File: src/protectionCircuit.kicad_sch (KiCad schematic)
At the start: 21 parts, among them M1 CSD19534Q5A, M2 CSD19534Q5A, M3 CSD19534Q5A, U1 LM74910QRGERQ1

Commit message: Restored powerDistribution PCB files to commit 2fb1c3a
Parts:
- removed M3: CSD19534Q5A, powerDristributionBoard-import-fps:DQJ8, symbol Schlib1:CSD19534Q5A
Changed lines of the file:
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@@
-	)
-	(symbol
-		(lib_id "Schlib1:CSD19534Q5A")
-		(at 233.68 20.32 0)
-		(unit 1)
-		(body_style 1)
-		(exclude_from_sim no)
-		(in_bom yes)
-		(on_board yes)
-		(in_pos_files yes)
-		(dnp no)
-		(property "Reference" "M3"
-			(at 241.3 20.32 0)
-			(show_name no)
-			(do_not_autoplace no)
-			(effects
-				(font
-					(size 1.27 1.27)
-				)
-				(justify left bottom)
-			)
-		)
-		(property "Value" "CSD19534Q5A"
-			(at 241.3 35.56 0)
-			(show_name no)
-			(do_not_autoplace no)
-			(effects
-				(font
-					(size 1.27 1.27)
-				)
-				(justify left bottom)
-			)
-		)
-		(property "Footprint" "powerDristributionBoard-import-fps:DQJ8"
-			(at 233.68 20.32 0)
-			(hide yes)
-			(show_name no)
-			(do_not_autoplace no)
-			(effects
-				(font
-					(size 1.27 1.27)
-				)
-			)
-		)
-		(property "Datasheet" ""
-			(at 233.68 20.32 0)
-			(hide yes)
-			(show_name no)
-			(do_not_autoplace no)
-			(effects
-				(font
-					(size 1.27 1.27)
-				)
-			)
-		)
-		(property "Description" "100-V, N channel NexFETâ„¢ power MOSFET, single SON 5 mm x 6 mm, 15.1 mOhm 8-VSONP -55 to 150"
-			(at 233.68 20.32 0)
-			(hide yes)
-			(show_name no)
-			(do_not_autoplace no)
-			(effects
-				(font
-					(size 1.27 1.27)
-				)
-			)
-		)
-		(property "COPYRIGHT" "Copyright (C) 2026 Ultra Librarian. All rights reserved."
-			(at 233.68 20.32 0)
-			(hide yes)
-			(show_name no)
-			(do_not_autoplace no)
-			(effects
-				(font
-					(size 1.27 1.27)
-				)
-				(justify left bottom)
-			)
-		)
-		(property "MANUFACTURER_NAME" "Texas Instruments"
-			(at 233.68 20.32 0)
-			(hide yes)
-			(show_name no)
-			(do_not_autoplace no)
-			(effects
-				(font
-					(size 1.27 1.27)
-				)
-				(justify left bottom)
-			)
-		)
-		(property "MANUFACTURER_PART_NUMBER" "CSD19534Q5A"
-			(at 233.68 20.32 0)
-			(hide yes)
-			(show_name no)
-			(do_not_autoplace no)
-			(effects
-				(font
-					(size 1.27 1.27)
-				)
-				(justify left bottom)
-			)
-		)
-		(property "REFDES" "RefDes"
-			(at 254 7.62 0)
-			(hide yes)
-			(show_name no)
-			(do_not_autoplace no)
-			(effects
-				(font
-					(size 1.27 1.27)
-				)
-				(justify left bottom)
-			)
-		)
-		(property "TYPE" "Type"
-			(at 254 10.16 0)
-			(hide yes)
-			(show_name no)
-			(do_not_autoplace no)
-			(effects
-				(font
-					(size 1.27 1.27)
-				)
-				(justify left bottom)
-			)
-		)
-		(pin "4"
-		)
-		(pin "1"
-		)
-		(pin "2"
-		)
-		(pin "3"
-		)
-		(pin "5"
-		)
-		(pin "6"
-		)
-		(pin "7"
-		)
-		(pin "8"
-		)
-		(instances
-			(project "powerDristributionBoard"
-				(path "/501e9f3f-9bfa-47dd-b56d-5fd6974f0d03/decf1042-8545-4374-a825-63213b68d513"
-					(reference "M3")
-					(unit 1)
-				)
-			)
-		)
 	)
 	(symbol

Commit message: Edited the protection circuit
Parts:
- added D1: TVS, symbol Diode:SMAJ6.5CA
- added R_IMON: 6.04k 1%, Resistor_SMD:R_0603_1608Metric, symbol Device:R_Small_US
- renumbered Ccs+1 to Ccs+, Cscp1 to Ciscp
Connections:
- net GND: now also D1.1 (A1), R_IMON.2
- net Vin: now also D1.2 (A2)
- net ENABLE: now reaches Ccap1.2, Cvs1.1, M1.5 (D), M1.6 (D), M1.7 (D), M1.8 (D), R18.1, R_ISCP1.1, Rset1.1, U1.22 (VS), U1.24 (C)
- net ENABLE: now also U1.6 (EN), U1.7 (*SLEEP)
- net Breakout Pin (For MCU): now reaches U1.10 (IMON)
- net Breakout Pin (For MCU): now also R_IMON.1
- no-connect marks 3 -> 5
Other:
- moved on the sheet: C_dvdt1, Ccap1, Ccs+, Ciscp, Cout1, Ctmr1, Cuv1, Cvin1, Cvs1, M1, M2, R18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

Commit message: Added many footprints
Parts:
- removed R18: 5mOhm, powerDristributionBoard-import-fps:CSNL2010, symbol Schlib1:CSNL2010
- added R18: 5mOhms, PowerPCB_Footprints:CSNL2010, symbol Device:R_Trim
- M1, M2: footprint powerDristributionBoard-import-fps:DQJ8 -> PowerPCB_Footprints:CSD19534Q5A
- U1: footprint powerDristributionBoard-import-fps:VQFN24_RGE-T_TEX-L -> PowerPCB_Footprints:LM74910QRGERQ1
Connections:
- net ENABLE: now also R18.1
- net at Ccs+.2, Ciscp.2, M2.1 (S)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: now also R18.2
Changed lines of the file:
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@@
 	(generator_version "10.0")
 	(paper "A")
+	(rectangle
+		(start 33.02 54.61)
+		(end 48.26 66.04)
+		(stroke
+			(width 0)
+			(type solid)
+			(color 255 8 21 1)
+		)
+		(fill
+			(type none)
+		)
+	)
+	(rectangle
+		(start 232.41 53.34)
+		(end 247.65 64.77)
+		(stroke
+			(width 0)
+			(type solid)
+			(color 255 8 21 1)
+		)
+		(fill
+			(type none)
+		)
+	)
 	(junction
 		(at 224.79 53.34)
@@
 	)
 	(junction
-		(at 194.31 50.8)
-		(diameter 0)
-		(color 0 0 0 0)
-	)
-	(junction
 		(at 165.1 91.44)
 		(diameter 0)
@@
 	)
 	(junction
-		(at 176.53 50.8)
-		(diameter 0)
-		(color 0 0 0 0)
-	)
-	(junction
 		(at 165.1 50.8)
 		(diameter 0)
@@
 	)
 	(junction
+		(at 176.53 50.8)
+		(diameter 0)
+		(color 0 0 0 0)
+	)
+	(junction
 		(at 49.53 106.68)
 		(diameter 0)
@@
 	)
 	(junction
+		(at 194.31 50.8)
+		(diameter 0)
+		(color 0 0 0 0)
+	)
+	(junction
 		(at 107.95 53.34)
 		(diameter 0)
@@
 	(wire
 		(pts
-			(xy 176.53 50.8) (xy 179.07 50.8)
+			(xy 176.53 50.8) (xy 181.61 50.8)
 		)
 		(stroke
@@
 	(wire
 		(pts
-			(xy 194.31 50.8) (xy 191.77 50.8)
+			(xy 194.31 50.8) (xy 189.23 50.8)
 		)
 		(stroke
@@
 			)
 		)
-		(property "Footprint" "powerDristributionBoard-import-fps:DQJ8"
+		(property "Footprint" "PowerPCB_Footprints:CSD19534Q5A"
 			(at 82.55 48.26 0)
 			(hide yes)
@@
 			)
 		)
-		(property "Footprint" "powerDristributionBoard-import-fps:DQJ8"
+		(property "Footprint" "PowerPCB_Footprints:CSD19534Q5A"
 			(at 199.39 48.26 0)
 			(hide yes)
@@
 	)
 	(symbol
-		(lib_id "Schlib1:CSNL2010")
-		(at 179.07 50.8 0)
+		(lib_id "Device:R_Small_US")
+		(at 165.1 72.39 0)
 		(unit 1)
 		(body_style 1)
@@
 		(in_pos_files yes)
 		(dnp no)
-		(property "Reference" "R18"
-			(at 181.356 49.276 0)
+		(fields_autoplaced yes)
+		(property "Reference" "R_ISCP1"
+			(at 167.64 71.1199 0)
 			(show_name no)
 			(do_not_autoplace no)
@@
 					(size 1.27 1.27)
 				)
-				(justify left bottom)
+				(justify left)
 			)
 		)
-		(property "Value" "5mOhm"
-			(at 181.61 55.88 0)
+		(property "Value" "952 1%"
+			(at 167.64 73.6599 0)
 			(show_name no)
 			(do_not_autoplace no)
@@
 					(size 1.27 1.27)
 				)
-				(justify left bottom)
+				(justify left)
 			)
 		)
-		(property "Footprint" "powerDristributionBoard-import-fps:CSNL2010"
-			(at 179.07 50.8 0)
+		(property "Footprint" "Resistor_SMD:R_0603_1608Metric"
+			(at 165.1 72.39 0)
 			(hide yes)
 			(show_name no)
@@
 		)
 		(property "Datasheet" ""
-			(at 179.07 50.8 0)
-			(hide yes)
-			(show_name no)
-			(do_not_autoplace no)
-			(effects
-				(font
-					(size 1.27 1.27)
-				)
-			)
-		)
-		(property "Description" ""
-			(at 179.07 50.8 0)
-			(hide yes)
-			(show_name no)
-			(do_not_autoplace no)
-			(effects
-				(font
-					(size 1.27 1.27)
-				)
-			)
-		)
-		(property "COPYRIGHT" "Copyright (C) 2025 Ultra Librarian. All rights reserved."
-			(at 179.07 50.8 0)
-			(hide yes)
-			(show_name no)
-			(do_not_autoplace no)
-			(effects
-				(font
-					(size 1.27 1.27)
-				)
-				(justify left bottom)
-			)
-		)
-		(property "MANUFACTURER_NAME" "Susumu"
-			(at 179.07 50.8 0)
-			(hide yes)
-			(show_name no)
-			(do_not_autoplace no)
-			(effects
-				(font
-					(size 1.27 1.27)
-				)
-				(justify left bottom)
-			)
-		)
-		(property "MANUFACTURER_PART_NUMBER" "PRL1632-R005-F-T1"
-			(at 179.07 50.8 0)
-			(hide yes)
-			(show_name no)
-			(do_not_autoplace no)
-			(effects
-				(font
-					(size 1.27 1.27)
-				)
-				(justify left bottom)
-			)
-		)
-		(property "TYPE" ""
-			(at 185.42 57.785 0)
+			(at 165.1 72.39 0)
 			(hide yes)
 			(show_name no)
@@
 					(size 1.27 1.27)
 				)
-				(justify left bottom)
 			)
 		)
-		(property "REFDES" ""
-			(at 184.785 46.99 0)
+		(property "Description" "Resistor, small US symbol"
+			(at 165.1 72.39 0)
 			(hide yes)
 			(show_name no)
@@
 					(size 1.27 1.27)
 				)
-				(justify left bottom)
 			)
 		)
@@
 			(project "powerDristributionBoard"
 				(path "/501e9f3f-9bfa-47dd-b56d-5fd6974f0d03/decf1042-8545-4374-a825-63213b68d513"
-					(reference "R18")
+					(reference "R_ISCP1")
 					(unit 1)
 				)
@@
 	)
 	(symbol
-		(lib_id "Device:R_Small_US")
-		(at 165.1 72.39 0)
+		(lib_id "Device:R_Trim")
+		(at 185.42 50.8 90)
 		(unit 1)
 		(body_style 1)
@@
 		(dnp no)
 		(fields_autoplaced yes)
-		(property "Reference" "R_ISCP1"
-			(at 167.64 71.1199 0)
+		(property "Reference" "R18"
+			(at 185.42 43.18 90)
 			(show_name no)
 			(do_not_autoplace no)
@@
 					(size 1.27 1.27)
 				)
-				(justify left)
 			)
 		)
-		(property "Value" "952 1%"
-			(at 167.64 73.6599 0)
+		(property "Value" "5mOhms"
+			(at 185.42 45.72 90)
 			(show_name no)
 			(do_not_autoplace no)
@@
 					(size 1.27 1.27)
 				)
-				(justify left)
 			)
 		)
-		(property "Footprint" "Resistor_SMD:R_0603_1608Metric"
-			(at 165.1 72.39 0)
+		(property "Footprint" "PowerPCB_Footprints:CSNL2010"
+			(at 185.42 52.578 90)
 			(hide yes)
 			(show_name no)
@@
 		)
 		(property "Datasheet" ""
-			(at 165.1 72.39 0)
+			(at 185.42 50.8 0)
 			(hide yes)
 			(show_name no)
@@
 			)
 		)
-		(property "Description" "Resistor, small US symbol"
-			(at 165.1 72.39 0)
+		(property "Description" "Trimmable resistor (preset resistor)"
+			(at 185.42 50.8 0)
 			(hide yes)
 			(show_name no)
@@
 			)
 		)
-		(pin "1"
-		)
 		(pin "2"
 		)
+		(pin "1"
+		)
 		(instances
 			(project "powerDristributionBoard"
 				(path "/501e9f3f-9bfa-47dd-b56d-5fd6974f0d03/decf1042-8545-4374-a825-63213b68d513"
-					(reference "R_ISCP1")
+					(reference "R18")
 					(unit 1)
 				)
@@
 			)
 		)
-		(property "Footprint" "powerDristributionBoard-import-fps:VQFN24_RGE-T_TEX-L"
+		(property "Footprint" "PowerPCB_Footprints:LM74910QRGERQ1"
 			(at 87.63 83.82 0)
 			(hide yes)

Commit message: Updated symbols
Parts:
- renumbered Ccs+ to Ccs+1, Ciscp to Ciscp1, R_IMON to R_IMON1
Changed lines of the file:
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@@
 		(dnp no)
 		(fields_autoplaced yes)
-		(property "Reference" "R_IMON"
+		(property "Reference" "R_IMON1"
 			(at 52.07 110.4899 0)
 			(show_name no)
@@
 			(project "powerDristributionBoard"
 				(path "/501e9f3f-9bfa-47dd-b56d-5fd6974f0d03/decf1042-8545-4374-a825-63213b68d513"
-					(reference "R_IMON")
+					(reference "R_IMON1")
 					(unit 1)
 				)
@@
 		(dnp no)
 		(fields_autoplaced yes)
-		(property "Reference" "Ciscp"
+		(property "Reference" "Ciscp1"
 			(at 185.4263 85.09 90)
 			(show_name no)
@@
 			(project "powerDristributionBoard"
 				(path "/501e9f3f-9bfa-47dd-b56d-5fd6974f0d03/decf1042-8545-4374-a825-63213b68d513"
-					(reference "Ciscp")
+					(reference "Ciscp1")
 					(unit 1)
 				)
@@
 		(dnp no)
 		(fields_autoplaced yes)
-		(property "Reference" "Ccs+"
+		(property "Reference" "Ccs+1"
 			(at 185.4263 72.39 90)
 			(show_name no)
@@
 			(project "powerDristributionBoard"
 				(path "/501e9f3f-9bfa-47dd-b56d-5fd6974f0d03/decf1042-8545-4374-a825-63213b68d513"
-					(reference "Ccs+")
-					(unit 1)
-				)
+					(reference "Ccs+1")
+					(unit 1)
+				)

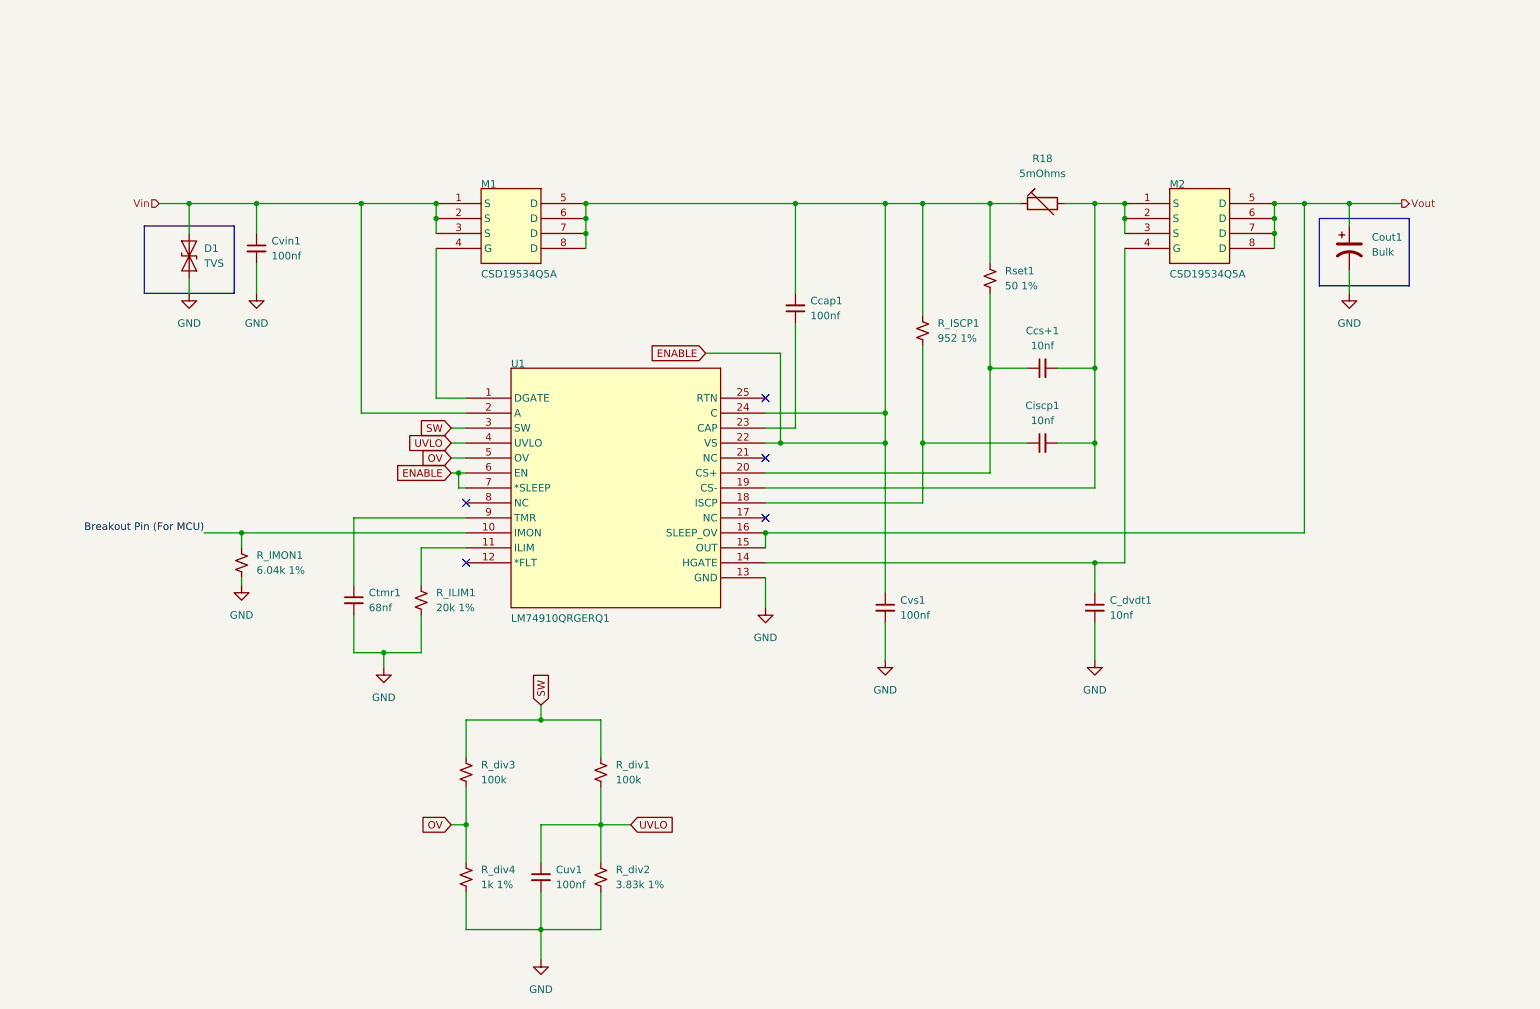
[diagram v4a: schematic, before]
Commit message: Redesigned 5V regulator and added more parts
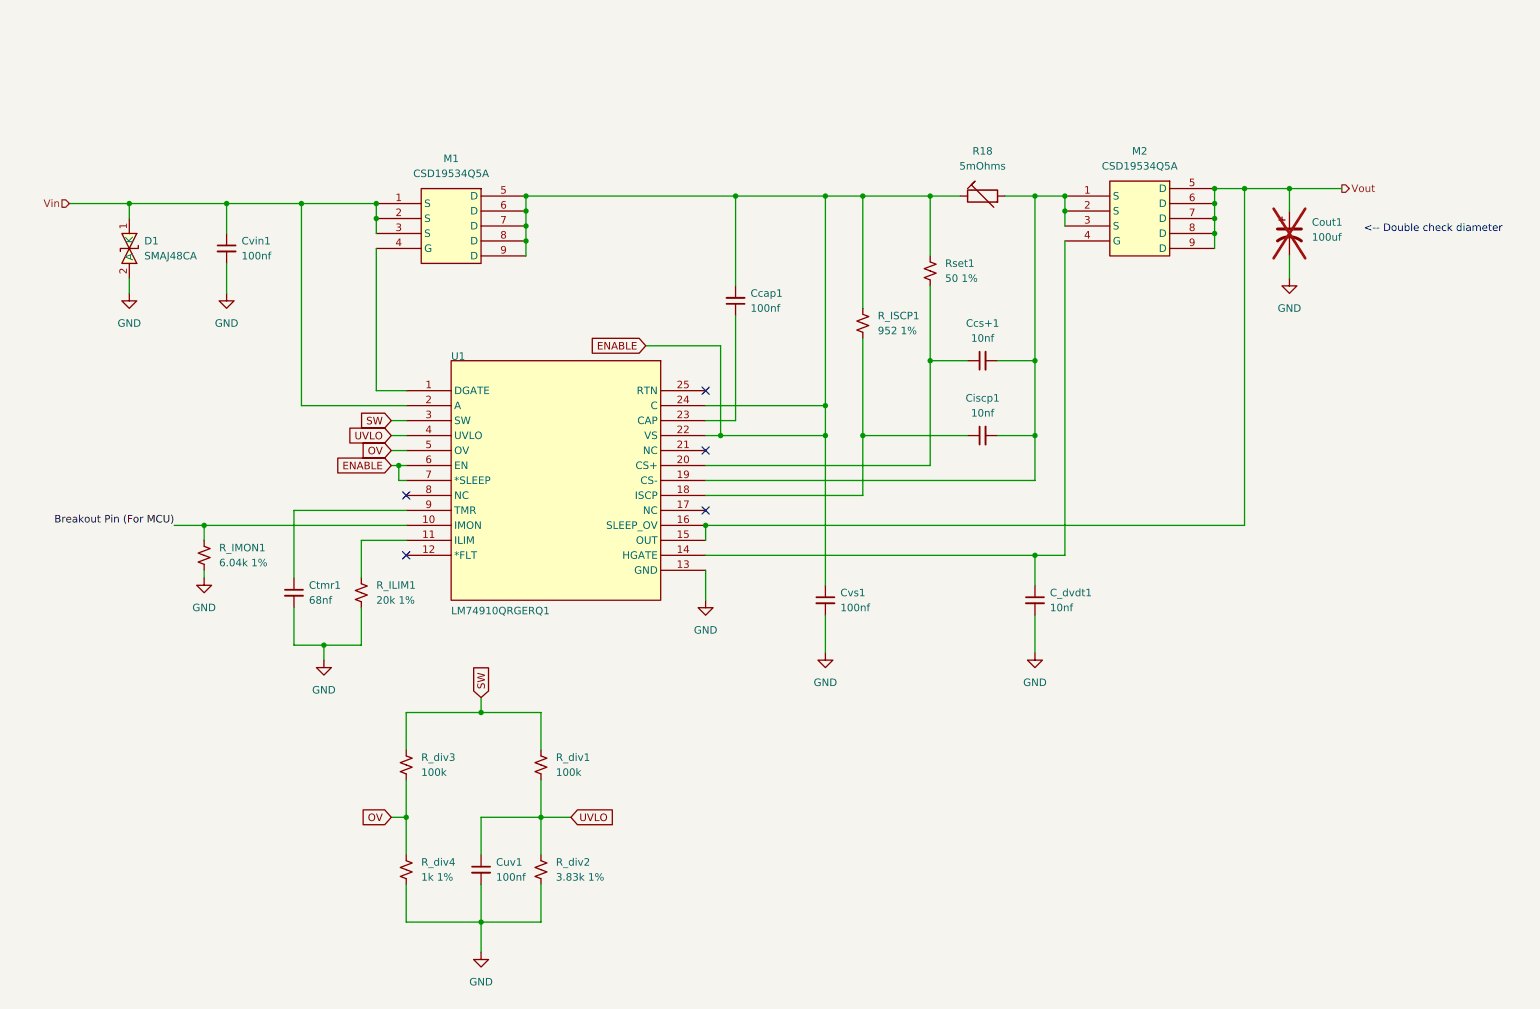
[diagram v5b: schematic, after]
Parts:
- removed D1: TVS, symbol Diode:SMAJ6.5CA
- removed M1, M2: CSD19534Q5A, PowerPCB_Footprints:CSD19534Q5A, symbol Schlib1:CSD19534Q5A
- added D1: SMAJ48CA, PowerPCB_Footprints:SMAJ48CA, symbol PowerPCB_Symbols:SMAJ48CA
- added M1, M2: CSD19534Q5A, PowerPCB_Footprints:CSD19534Q5A, symbol PowerPCB_Symbols:CSD19534Q5A
- Cout1: value Bulk -> 100uf; footprint (none) -> Capacitor_THT:CP_Radial_D7.5mm_P2.50mm; now not fitted
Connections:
- net ENABLE: now also M1.5 (D), M1.6 (D), M1.7 (D), M1.8 (D), M1.9 (D)
- net GND: now also D1.2 (A)
- net Vin: now also D1.1 (K), M1.1 (S), M1.2 (S), M1.3 (S)
- net Vout: now also M2.5 (D), M2.6 (D), M2.7 (D), M2.8 (D), M2.9 (D)
- net at U1.1 (DGATE): now also M1.4 (G)
- net at Ccs+1.2, Ciscp1.2, R18.2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: now also M2.1 (S), M2.2 (S), M2.3 (S)
- net at C_dvdt1.1, U1.14 (HGATE): now also M2.4 (G)
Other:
- note added: "<-- Double check diameter"
- moved on the sheet: C_dvdt1, Ccap1, Ccs+1, Ciscp1, Ctmr1, Cuv1, Cvin1, Cvs1, R18, R_ILIM1, R_IMON1, R_ISCP1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

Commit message: Finalized schematic
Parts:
- removed U1: LM74910QRGERQ1, PowerPCB_Footprints:LM74910QRGERQ1, symbol Schlib1:LM74910QRGERQ1
- added U1: LM74910QRGERQ1, PowerPCB_Footprints:LM74910QRGERQ1, symbol PowerPCB_Symbols:LM74910QRGERQ1
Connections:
- net Breakout Pin (For MCU): now also U1.10 (IMON)
- net ENABLE: now also U1.22 (VS), U1.24 (C), U1.6 (EN), U1.7 (*SLEEP)
- net GND: now also U1.13 (GND)
- net OV: now also U1.5 (OV)
- net SW: now also U1.3 (SW)
- net UVLO: now also U1.4 (UVLO)
- net Vin: now also U1.2 (A)
- net Vout: now also U1.15 (OUT), U1.16 (SLEEP_OV)
- net at Ccap1.1: now also U1.23 (CAP)
- net at Ctmr1.1: now also U1.9 (TMR)
- net at C_dvdt1.1, M2.4 (G): now also U1.14 (HGATE)
- net at Ciscp1.1, R_ISCP1.2: now also U1.18 (ISCP)
- net at Ccs+1.2, Ciscp1.2, M2.1 (S)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: now also U1.19 (CS-)
- net at Ccs+1.1, Rset1.2: now also U1.20 (CS+)
- net at M1.4 (G): now also U1.1 (DGATE)
- net at R_ILIM1.1: now also U1.11 (ILIM)
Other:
- moved on the sheet: Ccap1, Cuv1, R_div1, R_div2, R_div3, R_div4

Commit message: Edited PCB layout
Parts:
- renumbered Cvin1 to C1, Ctmr1 to C2, Cuv1 to C3, Ccap1 to C4, Cvs1 to C5, Ccs+1 to C6, Ciscp1 to C7, C_dvdt1 to C8, Cout1 to C9, R_IMON1 to R1, R_ILIM1 to R2, R_div3 to R3, R_div4 to R4, R_div1 to R5, R_div2 to R6, R_ISCP1 to R7, Rset1 to R8, R18 to R9

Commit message: Edited PCB layout
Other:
- moved on the sheet: C4
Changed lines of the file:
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@@
+	)
+	(junction
+		(at 133.35 49.53)
+		(diameter 0)
+		(color 0 0 0 0)
 	)
 	(junction
@@
 	(junction
 		(at 97.79 54.61)
-		(diameter 0)
-		(color 0 0 0 0)
-	)
-	(junction
-		(at 133.35 49.53)
 		(diameter 0)
 		(color 0 0 0 0)
@@
 	(wire
 		(pts
-			(xy 133.35 57.15) (xy 133.35 49.53)
+			(xy 133.35 67.31) (xy 133.35 49.53)
 		)
 		(stroke
@@
 	(wire
 		(pts
-			(xy 133.35 62.23) (xy 133.35 87.63)
+			(xy 133.35 72.39) (xy 133.35 87.63)
 		)
 		(stroke
@@
 	(symbol
 		(lib_id "Device:C_Small")
-		(at 133.35 59.69 180)
+		(at 133.35 69.85 180)
 		(unit 1)
 		(body_style 1)
@@
 		(fields_autoplaced yes)
 		(property "Reference" "C4"
-			(at 135.89 58.4135 0)
+			(at 135.89 68.5735 0)
 			(show_name no)
 			(do_not_autoplace no)
@@
 		)
 		(property "Value" "100nf"
-			(at 135.89 60.9535 0)
+			(at 135.89 71.1135 0)
 			(show_name no)
 			(do_not_autoplace no)
@@
 		)
 		(property "Footprint" "Capacitor_SMD:C_0603_1608Metric"
-			(at 133.35 59.69 0)
+			(at 133.35 69.85 0)
 			(hide yes)
 			(show_name no)
@@
 		)
 		(property "Datasheet" ""
-			(at 133.35 59.69 0)
+			(at 133.35 69.85 0)
 			(hide yes)
 			(show_name no)
@@
 		)
 		(property "Description" "Unpolarized capacitor, small symbol"
-			(at 133.35 59.69 0)
-			(hide yes)
-			(show_name no)
+			(at 133.35 69.85 0)
+			(hide yes)
+			(show_name no)
